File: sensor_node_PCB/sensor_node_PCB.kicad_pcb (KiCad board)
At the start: 2 copper layers, 47 parts, among them J1 USB_B_Mini, J2 INPUT CONNECTOR, J3 OUTPUT_CONNECTOR, P1 BREAKOUTS, Q1 FDN340P, Q2 BSS138, Q3 BSS138, SW1 RESET_SWITCH, U1 LMV358IDGKR, U2 LD1117S50TR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

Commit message: routing 50%
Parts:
- J1: footprint Connector_USB:USB_Mini-B_Wuerth_65100516121_Horizontal -> Connector_USB:USB_Mini-B_Tensility_54-00023_Vertical
- moved U7 103.4 mm to (139.4, 157.3), turned to 90 degrees
- moved C6 92.5 mm to (162.7, 168.9), turned to 90 degrees
- moved SW1 72.8 mm to (83.7, 152.4), turned to 45 degrees
- moved C5 69.5 mm to (135.8, 166.4), turned to 270 degrees
- moved R7 58.1 mm to (124.4, 168.3), turned to 90 degrees
- moved R9 49.9 mm to (124.9, 165.3), turned to 180 degrees
- moved R8 47.3 mm to (113.0, 160.9)
- moved C14 43.2 mm to (109.6, 156.3), turned to 270 degrees
- moved R2 40.9 mm to (102.1, 146.7)
- moved U8 40.4 mm to (129.1, 168.3), turned to 90 degrees
- moved R3 36.6 mm to (87.4, 140.8)
- moved U4 34.5 mm to (144.0, 161.8)
- moved C4 33.5 mm to (96.2, 146.3)
- moved D7 33.0 mm to (175.5, 149.7), turned to 90 degrees
- moved R6 31.4 mm to (109.7, 167.9), turned to 90 degrees
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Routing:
- net 5V_LDO: track 31.7 -> 99.6 mm
- net 3V3_LDO: track 0.00 -> 22.0 mm
- net /ARD_SCL_3V3: track 0.00 -> 20.3 mm
- net USBVCC: track 0.00 -> 19.0 mm
- net /USB_D-: track 0.00 -> 17.1 mm
- net /USB_D+: track 0.00 -> 12.4 mm
- net Net-(F1-Pad2): track 0.00 -> 10.7 mm
- net Net-(J1-Pad3): track 0.00 -> 8.16 mm
- net /ARD_SDA_3V3: track 0.00 -> 7.93 mm
- net Net-(R1-Pad1): track 0.00 -> 5.70 mm
- net 12V_BUS: track 0.00 -> 5.22 mm
- net /ARD_SDA: track 0.00 -> 4.86 mm
- net Vin: track 0.00 -> 4.29 mm
- net /atmega328p/328P_RESET: track 24.1 -> 28.4 mm
- net Net-(J1-Pad2): track 0.00 -> 4.12 mm
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
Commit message: routing 60% completed
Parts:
- added REF**: MountingHole_3mm_Pad, MountingHole:MountingHole_3mm_Pad, F.Cu at (187.5, 130.0)
- added REF**: MountingHole_3mm_Pad, MountingHole:MountingHole_3mm_Pad, F.Cu at (115.0, 130.0)
- added REF**: MountingHole_3mm_Pad, MountingHole:MountingHole_3mm_Pad, F.Cu at (187.5, 87.5)
- added REF**: MountingHole_3mm_Pad, MountingHole:MountingHole_3mm_Pad, F.Cu at (115.0, 87.5)
- moved R1 78.5 mm to (118.2, 112.8), turned to 180 degrees
- moved D1 73.4 mm to (112.8, 100.3), turned to 90 degrees
- moved R12 72.4 mm to (182.9, 113.5), turned to 180 degrees
- moved C2 70.6 mm to (111.1, 106.1)
- moved J2 58.4 mm to (104.1, 101.9)
- moved C6 55.8 mm to (182.8, 116.8), turned to 0 degrees
- moved R15 55.4 mm to (138.5, 115.3)
- moved R3 55.4 mm to (118.0, 94.6)
- moved Y1 55.4 mm to (156.6, 101.1)
- moved C4 55.4 mm to (126.8, 100.1)
- moved D2 55.4 mm to (112.4, 94.6)
- moved R7 55.4 mm to (155.0, 122.1)
- moved R9 55.4 mm to (155.5, 119.1)
- moved U2 55.4 mm to (162.8, 113.0)
- moved U4 55.4 mm to (174.6, 115.6)
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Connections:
- U6 pad 4: /AED_TX1 -> /ARD_TX1
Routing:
- net 5V_LDO: track 99.6 -> 139.3 mm
- net 3V3_LDO: track 22.0 -> 58.5 mm
- net /ARD_TX2: track 0.00 -> 33.5 mm, vias 0 -> 2
- net /ARD_RX2: track 0.00 -> 32.1 mm
- net /ARD_TX1: track 0.00 -> 31.1 mm
- net 12V_BUS: track 5.22 -> 32.9 mm
- net Net-(R1-Pad1): track 5.70 -> 28.2 mm
- net /ARD_RX1: track 0.00 -> 22.3 mm
- net Vin: track 4.29 -> 19.8 mm
- net Net-(D2-Pad2): track 0.00 -> 3.90 mm
- net /atmega328p/DTR: track 0.00 -> 3.25 mm
- net /atmega328p/328P_RESET: track 28.4 -> 30.9 mm
- net /atmega328p/ARD_DIG7: track 16.4 -> 14.3 mm
- net /atmega328p/ARD_DIG8: track 15.6 -> 13.6 mm
- net Net-(C11-Pad2): track 0.00 -> 1.80 mm
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
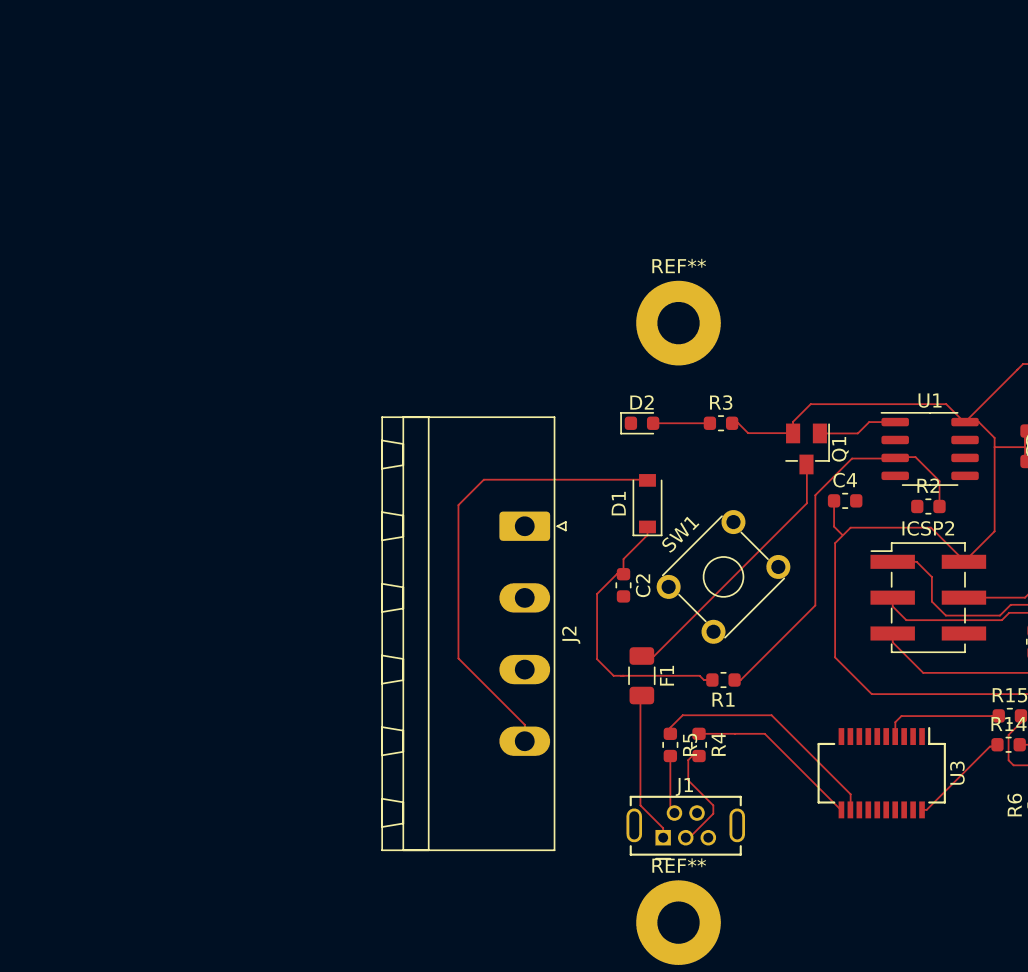
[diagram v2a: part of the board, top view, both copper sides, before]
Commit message: started placing mounting holes
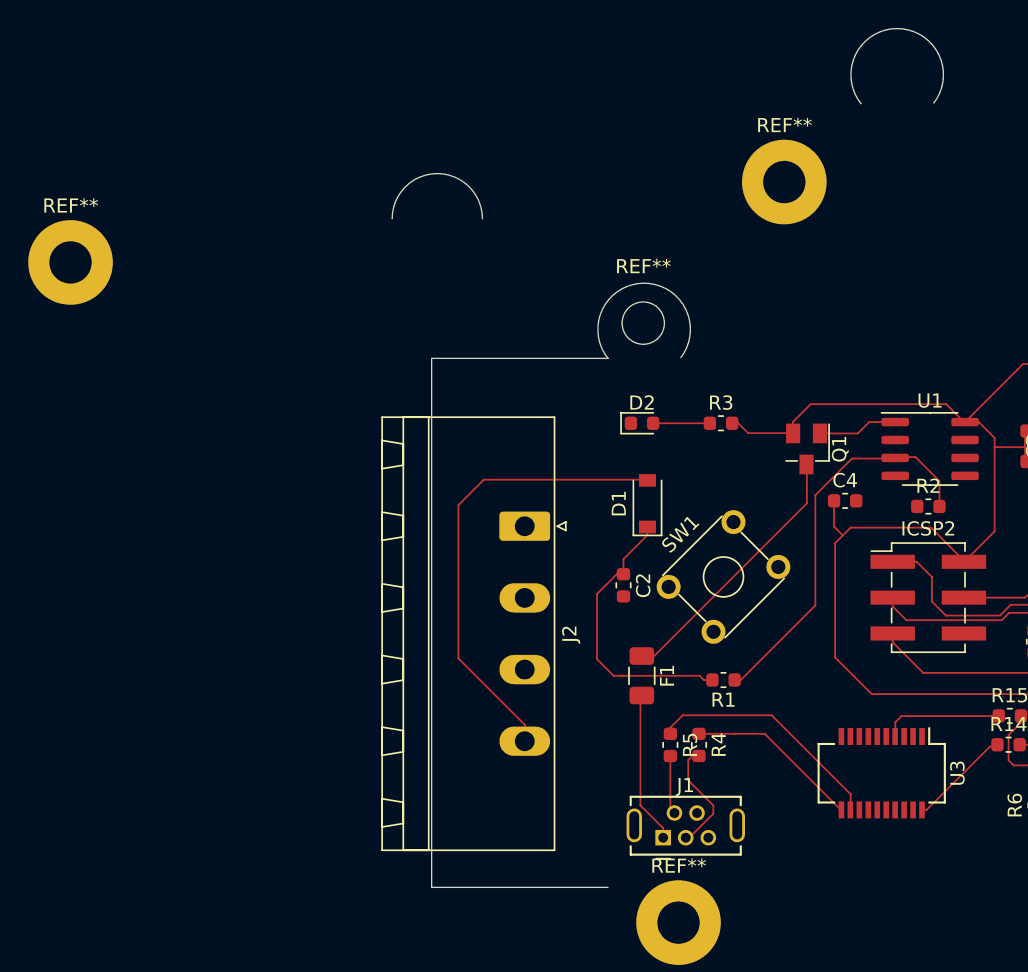
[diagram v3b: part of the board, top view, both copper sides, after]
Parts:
- removed the REF** at (115.0, 87.5)
- added REF**: MountingHole_3mm, MountingHole:MountingHole_3mm, F.Cu at (112.5, 87.5)
- added REF**: MountingHole_3mm_Pad, MountingHole:MountingHole_3mm_Pad, F.Cu at (71.9, 83.2)
- added REF**: MountingHole_3mm_Pad, MountingHole:MountingHole_3mm_Pad, F.Cu at (122.5, 77.5)
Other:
- board outline added: 39.1 x 60.9 mm
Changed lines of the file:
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@@
   (general
     (thickness 1.6)
-    (drawings 0)
+    (drawings 8)
     (tracks 280)
     (zones 0)
-    (modules 51)
+    (modules 53)
     (nets 64)
   )
@@
     (add_net Vin)
   )
+  (module MountingHole:MountingHole_3mm (layer F.Cu)
+    (at 112.5 87.5)
+    (descr "Mounting Hole 3mm, no annular")
+    (tags "mounting hole 3mm no annular")
+    (attr virtual)
+    (fp_text reference REF** (at 0 -4) (layer F.SilkS)
+      (effects (font (size 1 1) (thickness 0.15)))
+    )
+    (fp_text value MountingHole_3mm (at 0 4) (layer F.Fab)
+      (effects (font (size 1 1) (thickness 0.15)))
+    )
+    (fp_circle (center 0 0) (end 3.25 0) (layer F.CrtYd) (width 0.05))
+    (fp_circle (center 0 0) (end 3 0) (layer Cmts.User) (width 0.15))
+    (fp_text user %R (at 0.3 0) (layer F.Fab)
+      (effects (font (size 1 1) (thickness 0.15)))
+    )
+    (pad 1 np_thru_hole circle (at 0 0) (size 3 3) (drill 3) (layers *.Cu *.Mask))
+  )
+  (module MountingHole:MountingHole_3mm_Pad (layer F.Cu)
+    (at 71.9 83.2)
+    (descr "Mounting Hole 3mm")
+    (tags "mounting hole 3mm")
+    (attr virtual)
+    (fp_text reference REF** (at 0 -4) (layer F.SilkS)
+      (effects (font (size 1 1) (thickness 0.15)))
+    )
+    (fp_text value MountingHole_3mm_Pad (at 0 4) (layer F.Fab)
+      (effects (font (size 1 1) (thickness 0.15)))
+    )
+    (fp_text user %R (at 0.3 0) (layer F.Fab)
+      (effects (font (size 1 1) (thickness 0.15)))
+    )
+    (fp_circle (center 0 0) (end 3 0) (layer Cmts.User) (width 0.15))
+    (fp_circle (center 0 0) (end 3.25 0) (layer F.CrtYd) (width 0.05))
+    (pad 1 thru_hole circle (at 0 0) (size 6 6) (drill 3) (layers *.Cu *.Mask))
+  )
   (module MountingHole:MountingHole_3mm_Pad (layer F.Cu)
     (at 187.5 130)
@@
   )
   (module MountingHole:MountingHole_3mm_Pad (layer F.Cu)
-    (at 115 87.5)
+    (at 122.5 77.5)
     (descr "Mounting Hole 3mm")
     (tags "mounting hole 3mm")
@@
     )
   )
+  (gr_arc (start 130.5 69.9) (end 133.099999 71.899999) (angle -256.2284003) (layer Edge.Cuts) (width 0.05))
+  (gr_arc (start 112.561439 87.950849) (end 115.161438 89.950848) (angle -256.2284003) (layer Edge.Cuts) (width 0.05))
+  (gr_arc (start 97.9 80.1) (end 101.1 80.1) (angle -180) (layer Edge.Cuts) (width 0.05))
+  (dimension 6.5 (width 0.15) (layer Dwgs.User)
+    (gr_text "6.500 mm" (at 97.5 83.8) (layer Dwgs.User)
+      (effects (font (size 1 1) (thickness 0.15)))
+    )
+    (feature1 (pts (xy 100.75 82.5) (xy 100.75 83.086421)))
+    (feature2 (pts (xy 94.25 82.5) (xy 94.25 83.086421)))
+    (crossbar (pts (xy 94.25 82.5) (xy 100.75 82.5)))
+    (arrow1a (pts (xy 100.75 82.5) (xy 99.623496 83.086421)))
+    (arrow1b (pts (xy 100.75 82.5) (xy 99.623496 81.913579)))
+    (arrow2a (pts (xy 94.25 82.5) (xy 95.376504 83.086421)))
+    (arrow2b (pts (xy 94.25 82.5) (xy 95.376504 81.913579)))
+  )
+  (dimension 6.5 (width 0.15) (layer Dwgs.User)
+    (gr_text "6.500 mm" (at 97.5 83.8) (layer Dwgs.User)
+      (effects (font (size 1 1) (thickness 0.15)))
+    )
+    (feature1 (pts (xy 100.75 82.5) (xy 100.75 83.086421)))
+    (feature2 (pts (xy 94.25 82.5) (xy 94.25 83.086421)))
+    (crossbar (pts (xy 94.25 82.5) (xy 100.75 82.5)))
+    (arrow1a (pts (xy 100.75 82.5) (xy 99.623496 83.086421)))
+    (arrow1b (pts (xy 100.75 82.5) (xy 99.623496 81.913579)))
+    (arrow2a (pts (xy 94.25 82.5) (xy 95.376504 83.086421)))
+    (arrow2b (pts (xy 94.25 82.5) (xy 95.376504 81.913579)))
+  )
+  (gr_line (start 97.5 127.5) (end 110 127.5) (layer Edge.Cuts) (width 0.05))
+  (gr_line (start 97.5 90) (end 97.5 127.5) (layer Edge.Cuts) (width 0.05))
+  (gr_line (start 110 90) (end 97.5 90) (layer Edge.Cuts) (width 0.05))
   (segment (start 136.285 94.516) (end 137.407 95.638) (width 0.127) (layer F.Cu) (net 1))
   (segment (start 135.31 94.516) (end 136.285 94.516) (width 0.127) (layer F.Cu) (net 1))

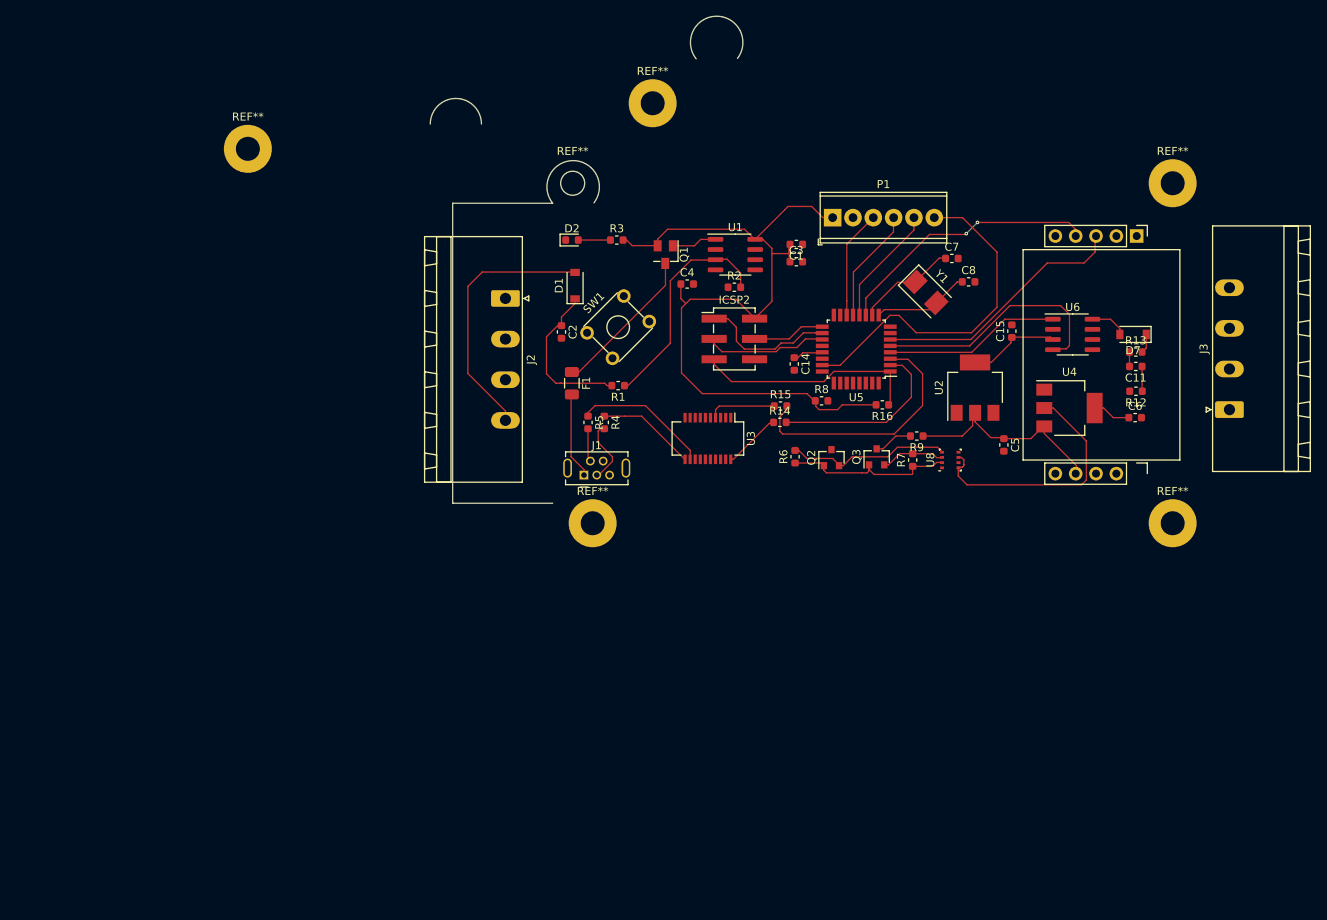
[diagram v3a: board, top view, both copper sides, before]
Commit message: edge cuts layer with mounting holes complete
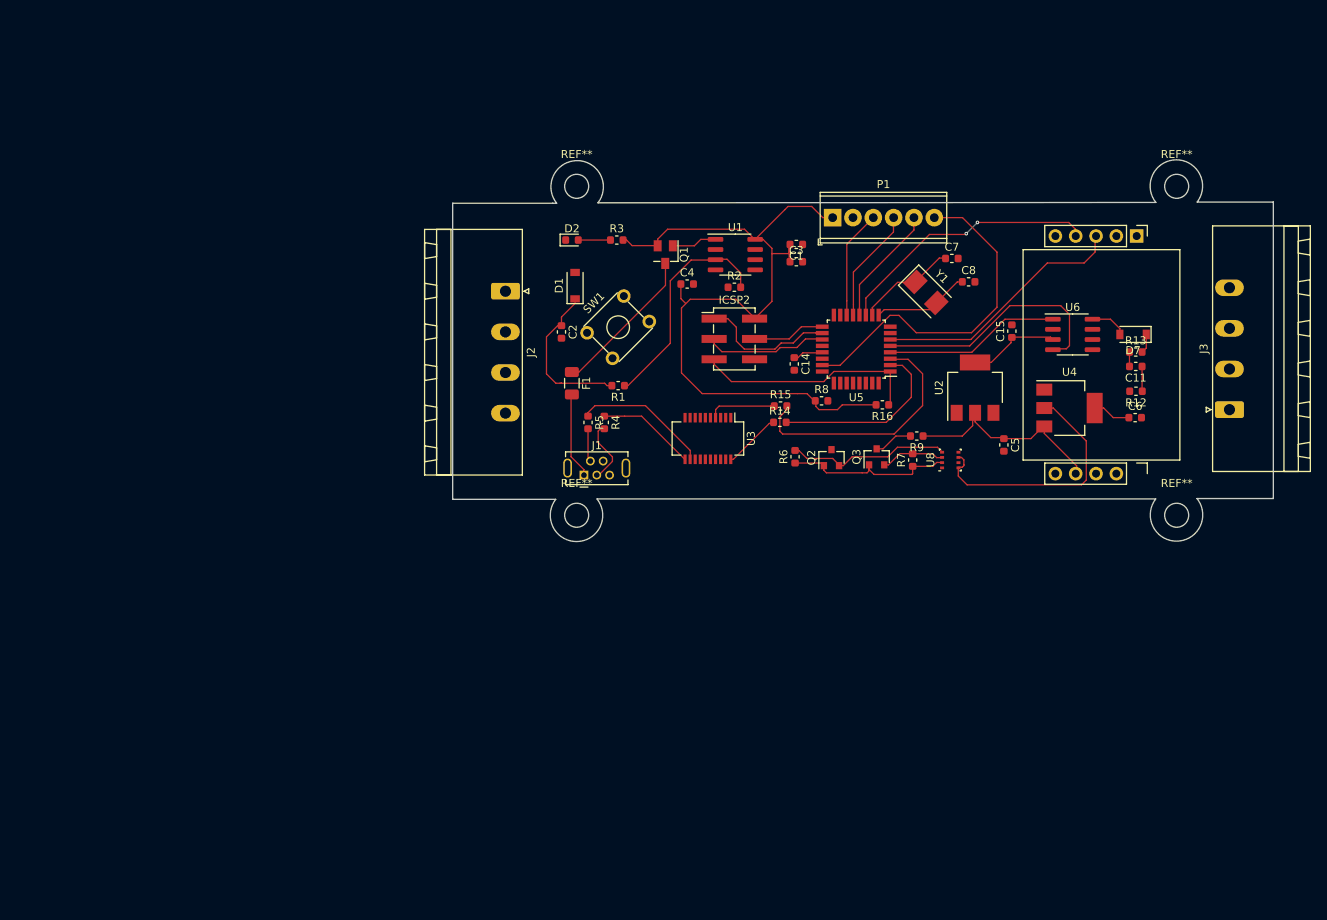
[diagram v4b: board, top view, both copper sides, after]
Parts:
- removed the REF** at (112.5, 87.5)
- removed the REF** at (71.9, 83.2)
- removed the REF** at (187.5, 130.0)
- removed the REF** at (115.0, 130.0)
- removed the REF** at (187.5, 87.5)
- removed the REF** at (122.5, 77.5)
- added REF**: MountingHole_3mm, MountingHole:MountingHole_3mm, F.Cu at (113.0, 129.0)
- added REF**: MountingHole_3mm, MountingHole:MountingHole_3mm, F.Cu at (188.0, 129.0)
- added REF**: MountingHole_3mm, MountingHole:MountingHole_3mm, F.Cu at (188.0, 87.9)
- added REF**: MountingHole_3mm, MountingHole:MountingHole_3mm, F.Cu at (113.0, 87.9)
- moved J2 0.90 mm to (104.1, 101.0)
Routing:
- net 12V_BUS: track 32.9 -> 0.08 mm
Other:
- board size 39.1 x 60.9 mm -> 102.6 x 47.7 mm

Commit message: routing complete
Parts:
- moved R5 4.77 mm to (118.6, 115.2), turned to 180 degrees
- moved R9 2.97 mm to (158.5, 119.4)
- moved R4 2.45 mm to (118.8, 116.6), turned to 180 degrees
- moved J1 2.39 mm to (113.4, 121.6)
- moved R13 1.26 mm to (182.9, 109.9)
- moved C11 1.23 mm to (182.9, 111.6)
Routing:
- net /MODBUS_B+: track 0.00 -> 166.5 mm
- net /MODBUS_A-: track 0.00 -> 151.0 mm, vias 0 -> 1
- net 5V_LDO: track 139.3 -> 276.4 mm, vias 0 -> 5
- net 12V_BUS: track 0.08 -> 135.2 mm
- net 3V3_LDO: track 58.5 -> 152.8 mm
- net Vin: track 19.8 -> 102.1 mm, vias 0 -> 2
- net /atmega328p/328P_RESET: track 30.9 -> 82.6 mm, vias 0 -> 4
- net /ARD_SDA: track 4.86 -> 18.8 mm, vias 0 -> 2
- net /ARD_SCL: track 0.00 -> 13.5 mm, vias 0 -> 2
- net Net-(U3-Pad13): track 0.00 -> 7.11 mm, vias 0 -> 2
- net /USB_D-: track 17.1 -> 11.3 mm
- net /USB_D+: track 12.4 -> 9.25 mm
- net Net-(F1-Pad2): track 10.7 -> 8.11 mm
- net Net-(J1-Pad2): track 4.12 -> 6.38 mm
- net GND: track 0.00 -> 2.18 mm, vias 0 -> 10
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- added copper zone on B.Cu, net GND
- added copper zone on F.Cu, net GND
